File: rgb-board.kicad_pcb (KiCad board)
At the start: 2 copper layers, 178 x 129.5 mm, 84 parts, among them J1 Conn_02x25_Odd_Even, J10 Conn_Coaxial, J11 Conn_Coaxial, J2 SCART-F, J3 TEST_1P, J4 TEST_1P, Q101 BC850C, Q105 BC850C, Q109 BC850C, Q113 BC850C, Q114 BC850C, Q201 BC850C, SW1 SW_DPDT_x2, U1 NCP1117-12_SOT223

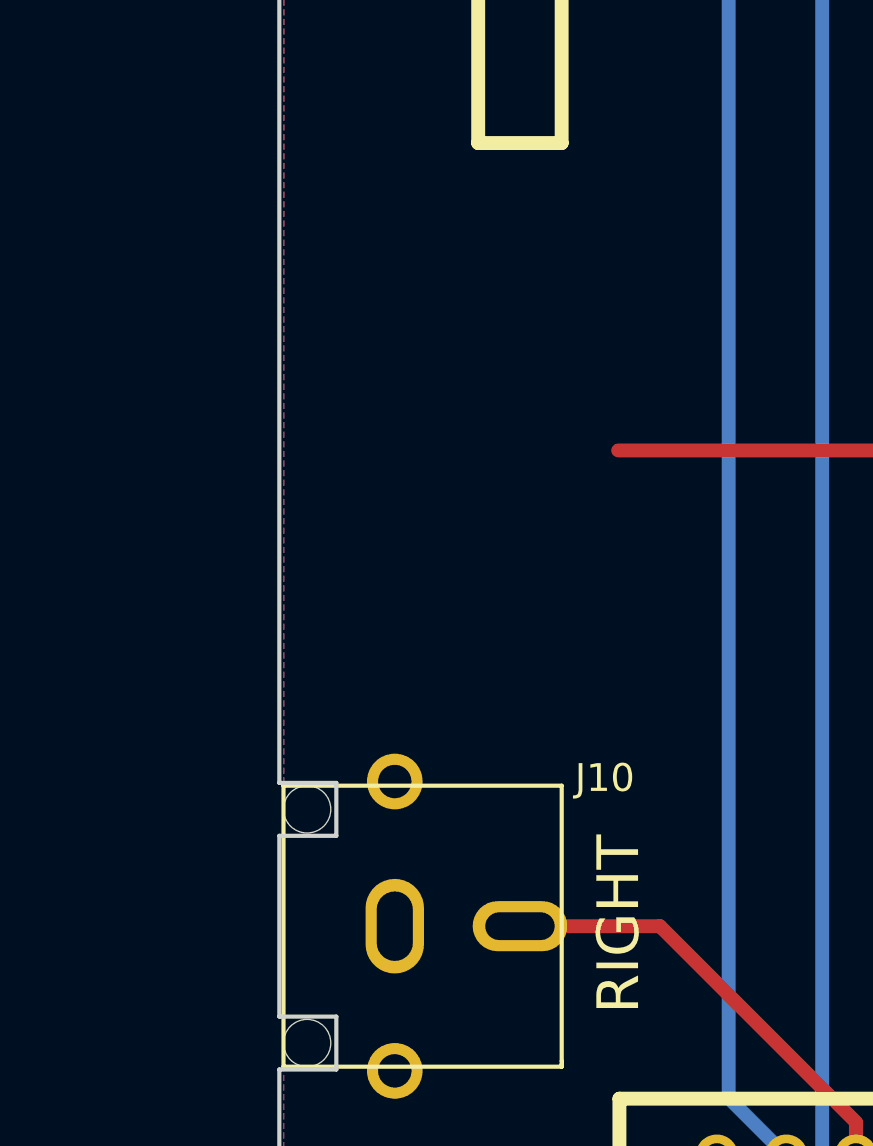
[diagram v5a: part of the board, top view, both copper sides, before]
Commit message: Add DSUB-15 VGA Connector. Custom footprint from https://github.com/skumlos/bkm-129x-scart-vga Note pins rows spacing 2.54 mm.
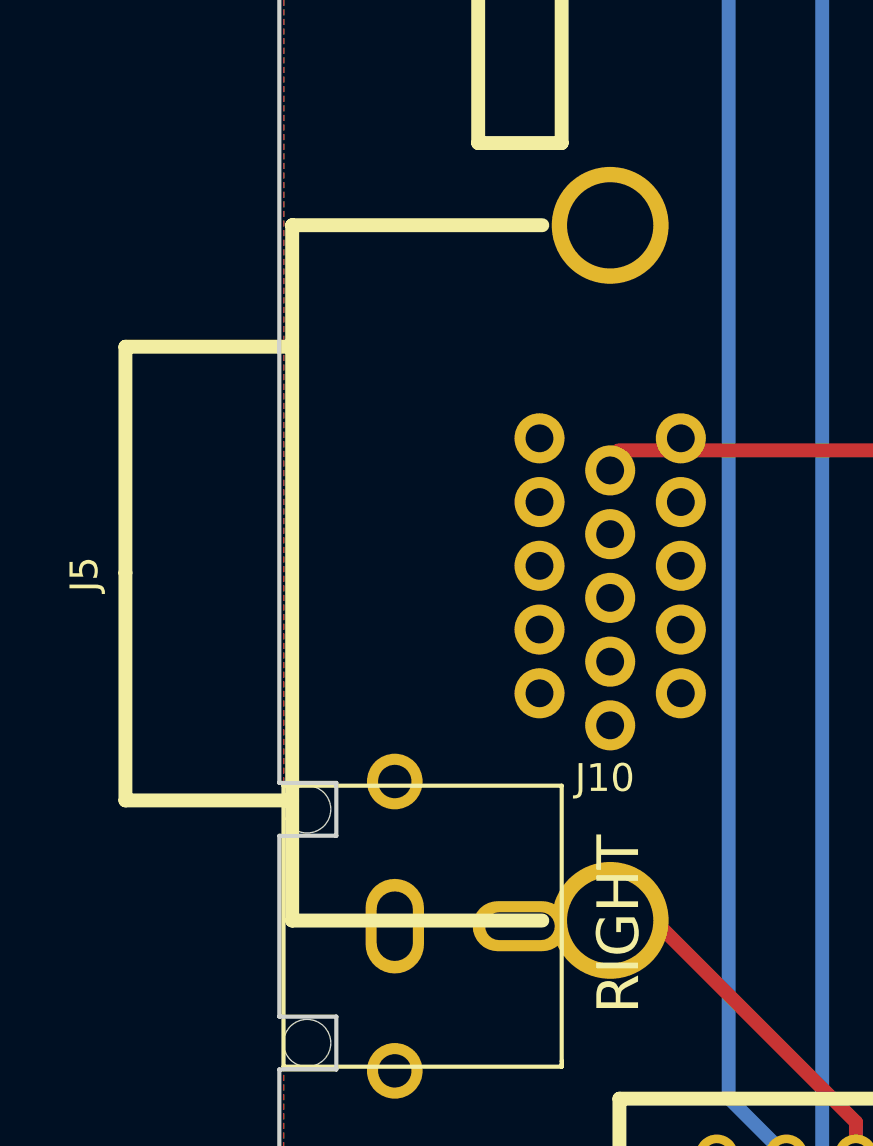
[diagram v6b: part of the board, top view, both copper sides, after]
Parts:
- added J5: DE15_Plug_HighDensity_MountingHoles, HD15-VGA:HD15-VGA, F.Cu at (61.7, 117.8)

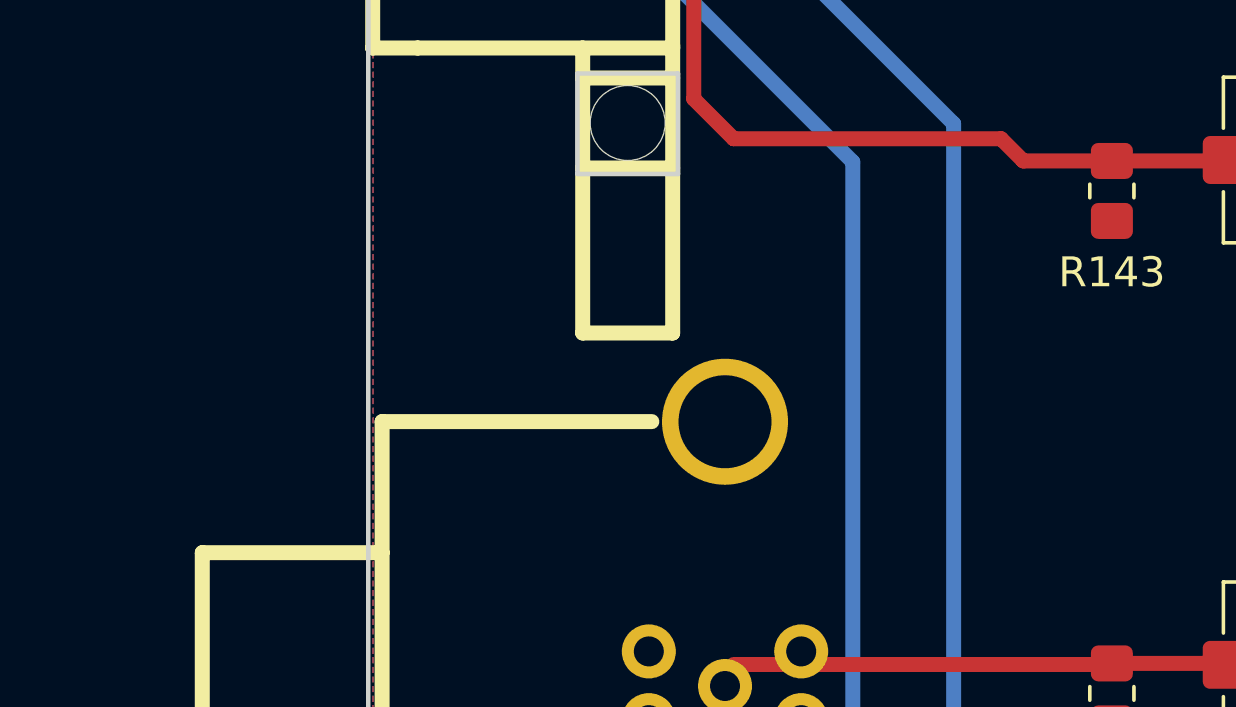
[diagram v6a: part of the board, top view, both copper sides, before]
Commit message: Add ALPS SPUJ Series SPUJ193700 4PDT switch. Custom Push Button 4PDT symbol from https://github.com/skumlos/bkm-129x-scart-vga Custom E-Switch PBH4UEE 4PDT switch footprint from https://github.com/skumlos/bkm-129x-scart-vga
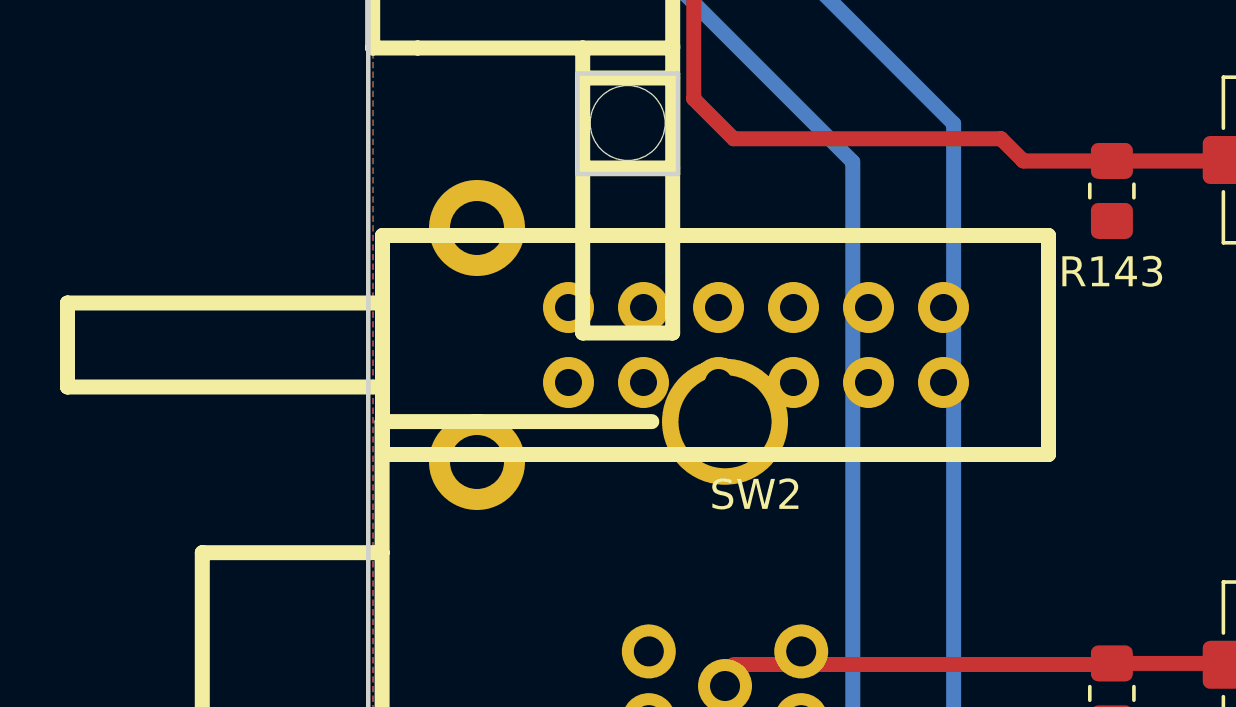
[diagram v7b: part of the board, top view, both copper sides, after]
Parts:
- added SW2: SPUJ193700, PBH4UEE:PBH4UEE, F.Cu at (62.8, 102.8)

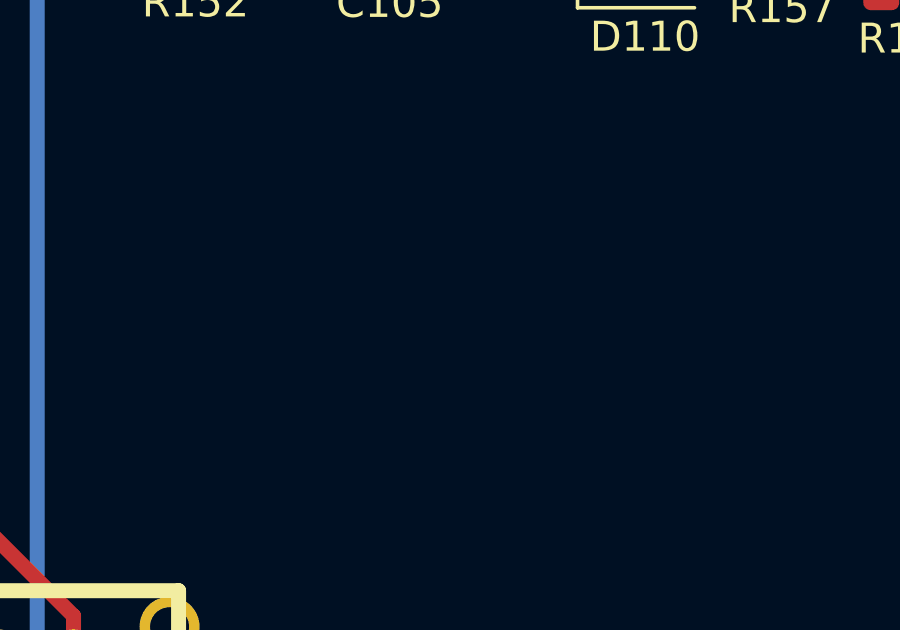
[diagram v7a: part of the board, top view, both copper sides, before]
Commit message: Add OMRON G6K-2PY-12DC Miniature Relay Dual Pole DPDT.
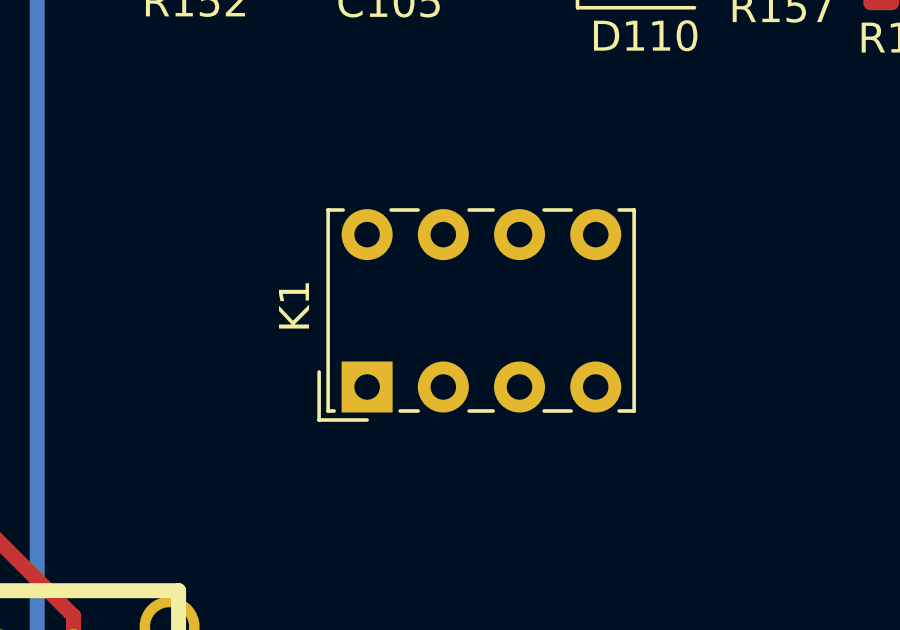
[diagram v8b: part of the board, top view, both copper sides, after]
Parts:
- added K1: G6K-2PY-12DC, Relay_THT:Relay_DPDT_Omron_G6K-2P, F.Cu at (80.3, 129.9)
